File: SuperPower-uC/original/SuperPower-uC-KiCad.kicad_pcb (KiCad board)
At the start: 2 copper layers, 90 x 90 mm, 160 parts, among them J1 JST_PH_S2B_thru, J2 DNP/JST_ZH_S2B_thru, J3 JST_XH_S2B_thru, J4 mcu_pinout, J5 mcu_pinout, J601 Conn_01x02_Male, J8 Barrel_Jack_Switch, J9 DNP/Screw_Terminal_01x02, Q1 DMN2019UTS, Q2 DMN3018SSD, Q3 2N7002A, Q4 DMP3028LSD, Q5 S8050, Q6 S8050, Q7 2N7002A, Q701 DMP3028LSD, Q702 DMN3018SSD, Q703 2N7002A, Q8 DMP3028LSD, Q9 2N7002A, SW1 DNP/SKRKAEE020, U1 AP9101CK6-AYTRG1, U2 LTC4162EUFD-LAD, U3 USB-C, U4 CP2102N-A01-GQFN28, U5 ESP32-WROOM32, U601 RV-3028-C7, U701 TPS63070RNMT, U702 TPS63070RNMT, U703 TPS70933DRVT, U9 IP4220CZ6

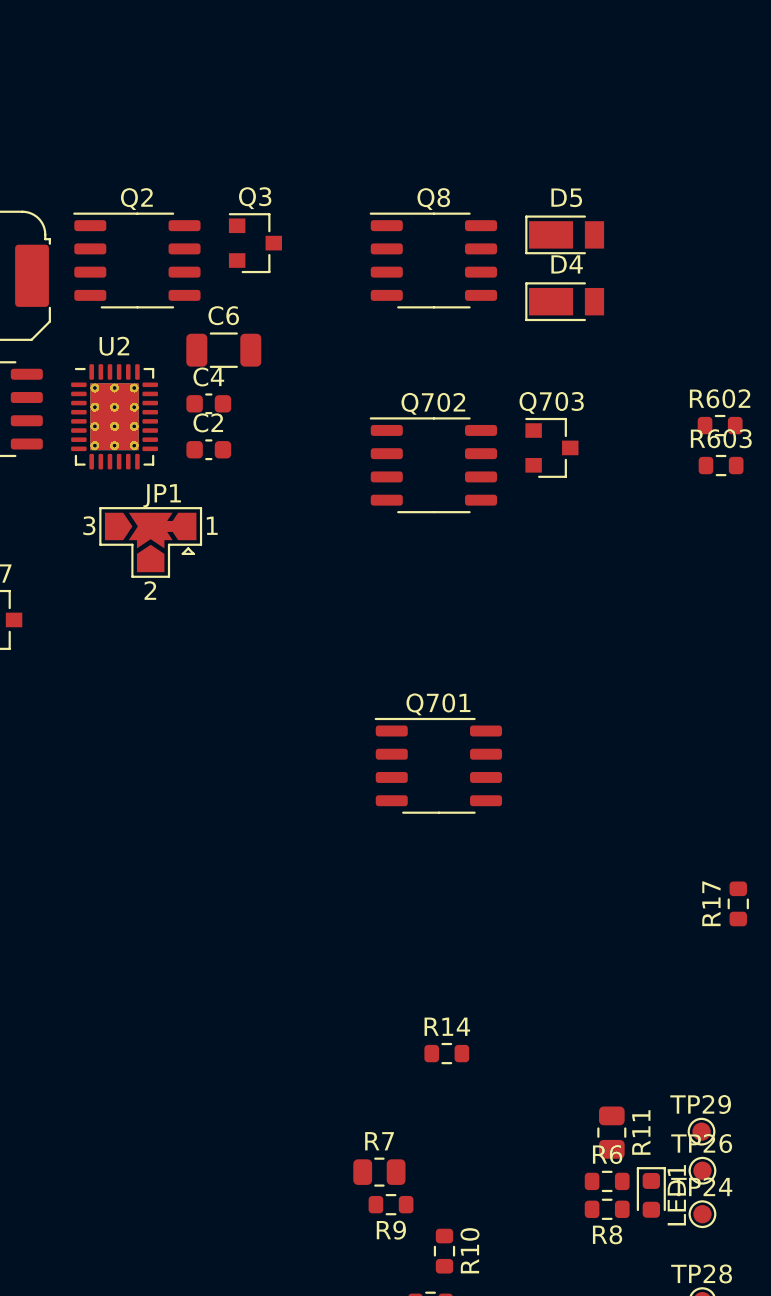
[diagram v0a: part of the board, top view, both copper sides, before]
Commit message: Update LTC4162-L Rsenses
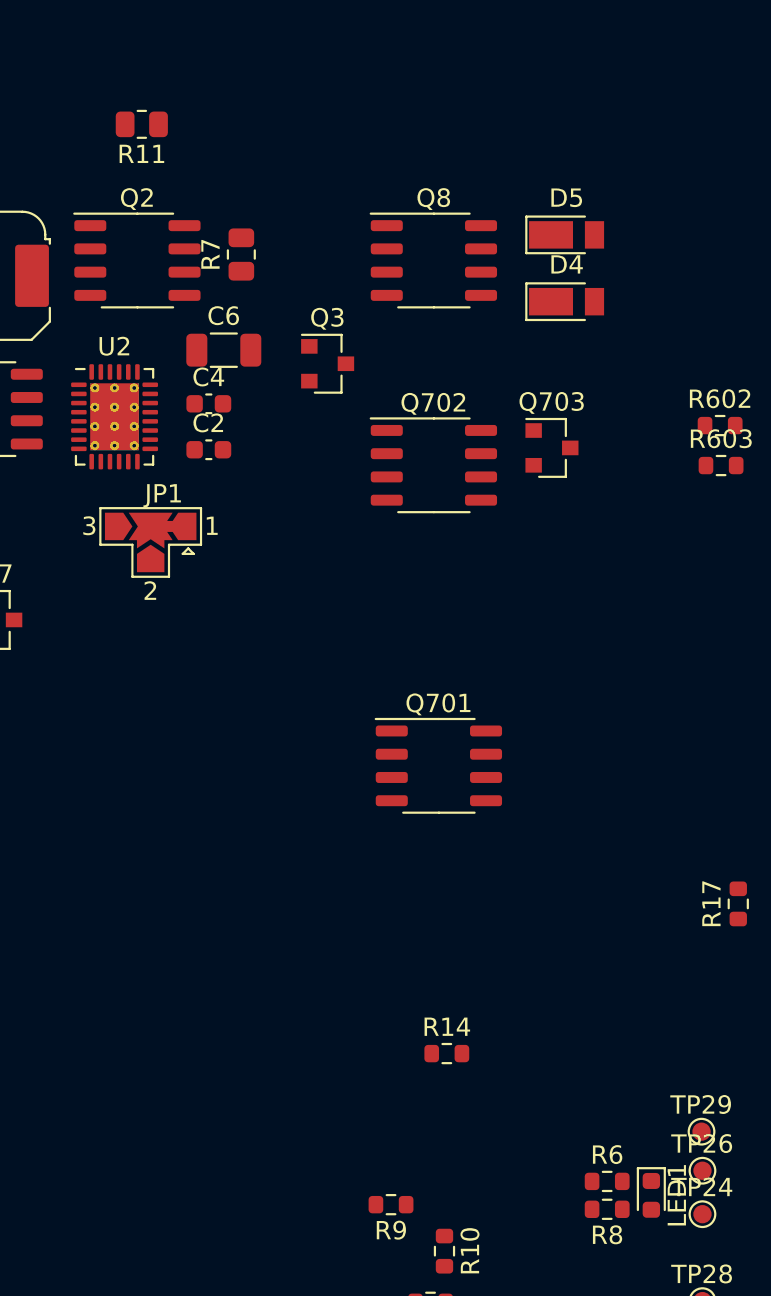
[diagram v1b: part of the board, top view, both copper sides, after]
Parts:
- R11, R7: value 68m -> RL0805FR-7W0R068L
- moved R11 60.8 mm to (68.1, 37.7), turned to 180 degrees
- moved R7 50.7 mm to (73.5, 44.8), turned to 90 degrees
- moved Q3 7.68 mm to (78.2, 50.8)
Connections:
- R11 pad 1: Net-(L1-Pad2) -> +BATT
- R11 pad 2: +BATT -> Net-(L1-Pad2)

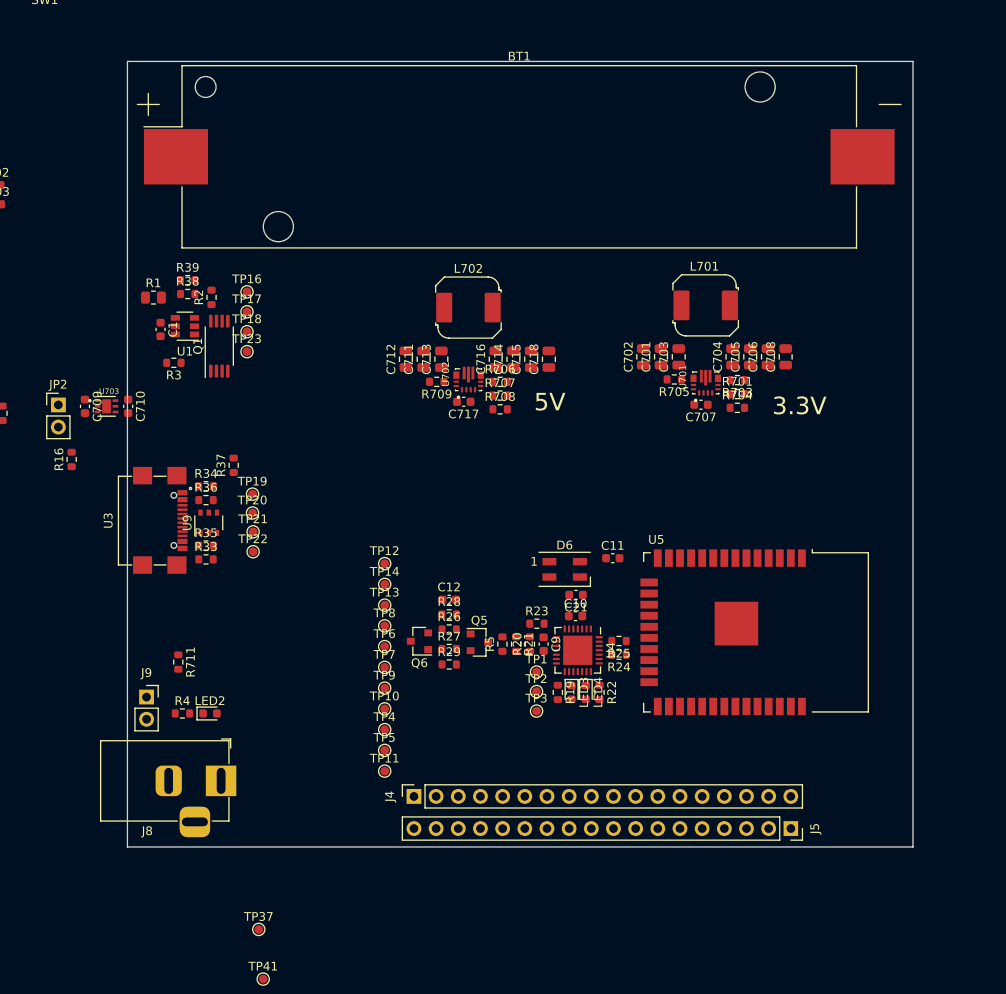
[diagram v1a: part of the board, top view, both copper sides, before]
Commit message: Add 3.2mm Mounting Holes (x4)
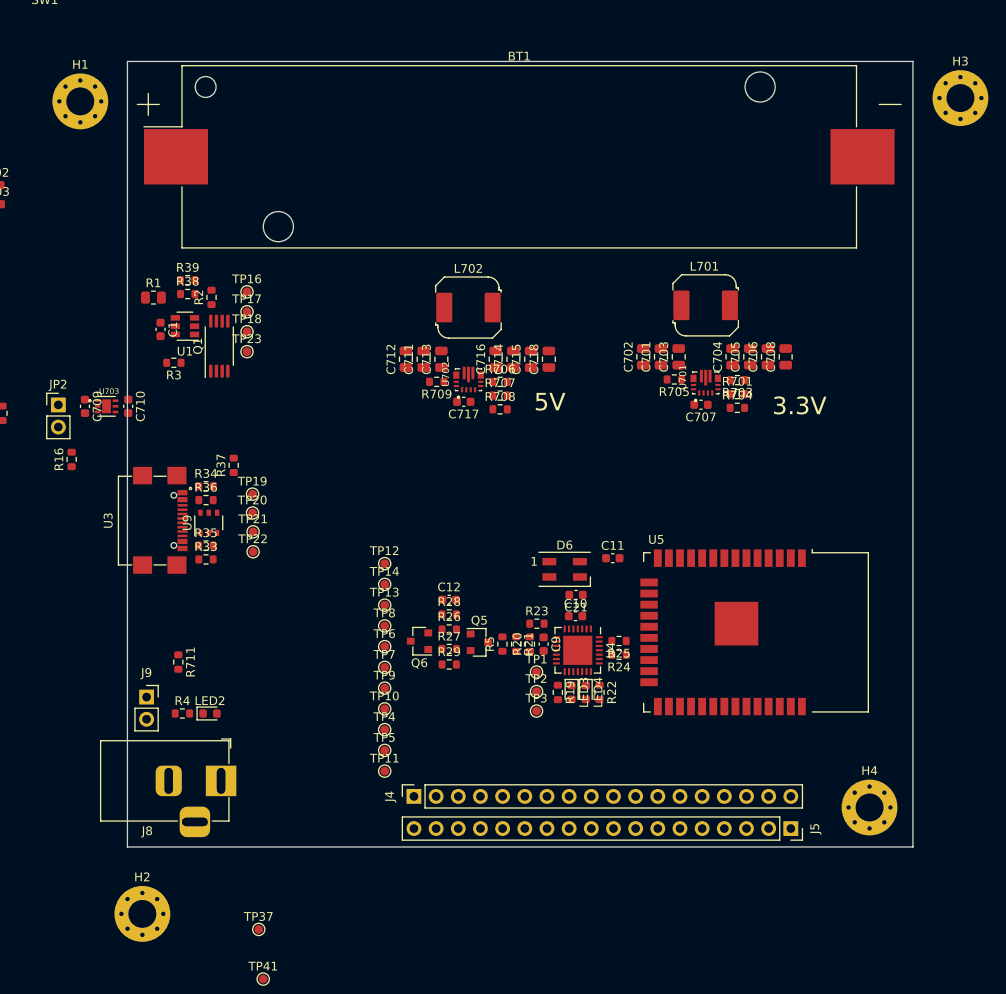
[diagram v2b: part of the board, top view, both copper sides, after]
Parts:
- added H1: MountingHole_Pad, MountingHole:MountingHole_3.2mm_M3_Pad_Via, F.Cu at (109.6, 44.6)
- added H2: MountingHole_Pad, MountingHole:MountingHole_3.2mm_M3_Pad_Via, F.Cu at (116.7, 137.7)
- added H3: MountingHole_Pad, MountingHole:MountingHole_3.2mm_M3_Pad_Via, F.Cu at (210.4, 44.2)
- added H4: MountingHole_Pad, MountingHole:MountingHole_3.2mm_M3_Pad_Via, F.Cu at (200.0, 125.5)

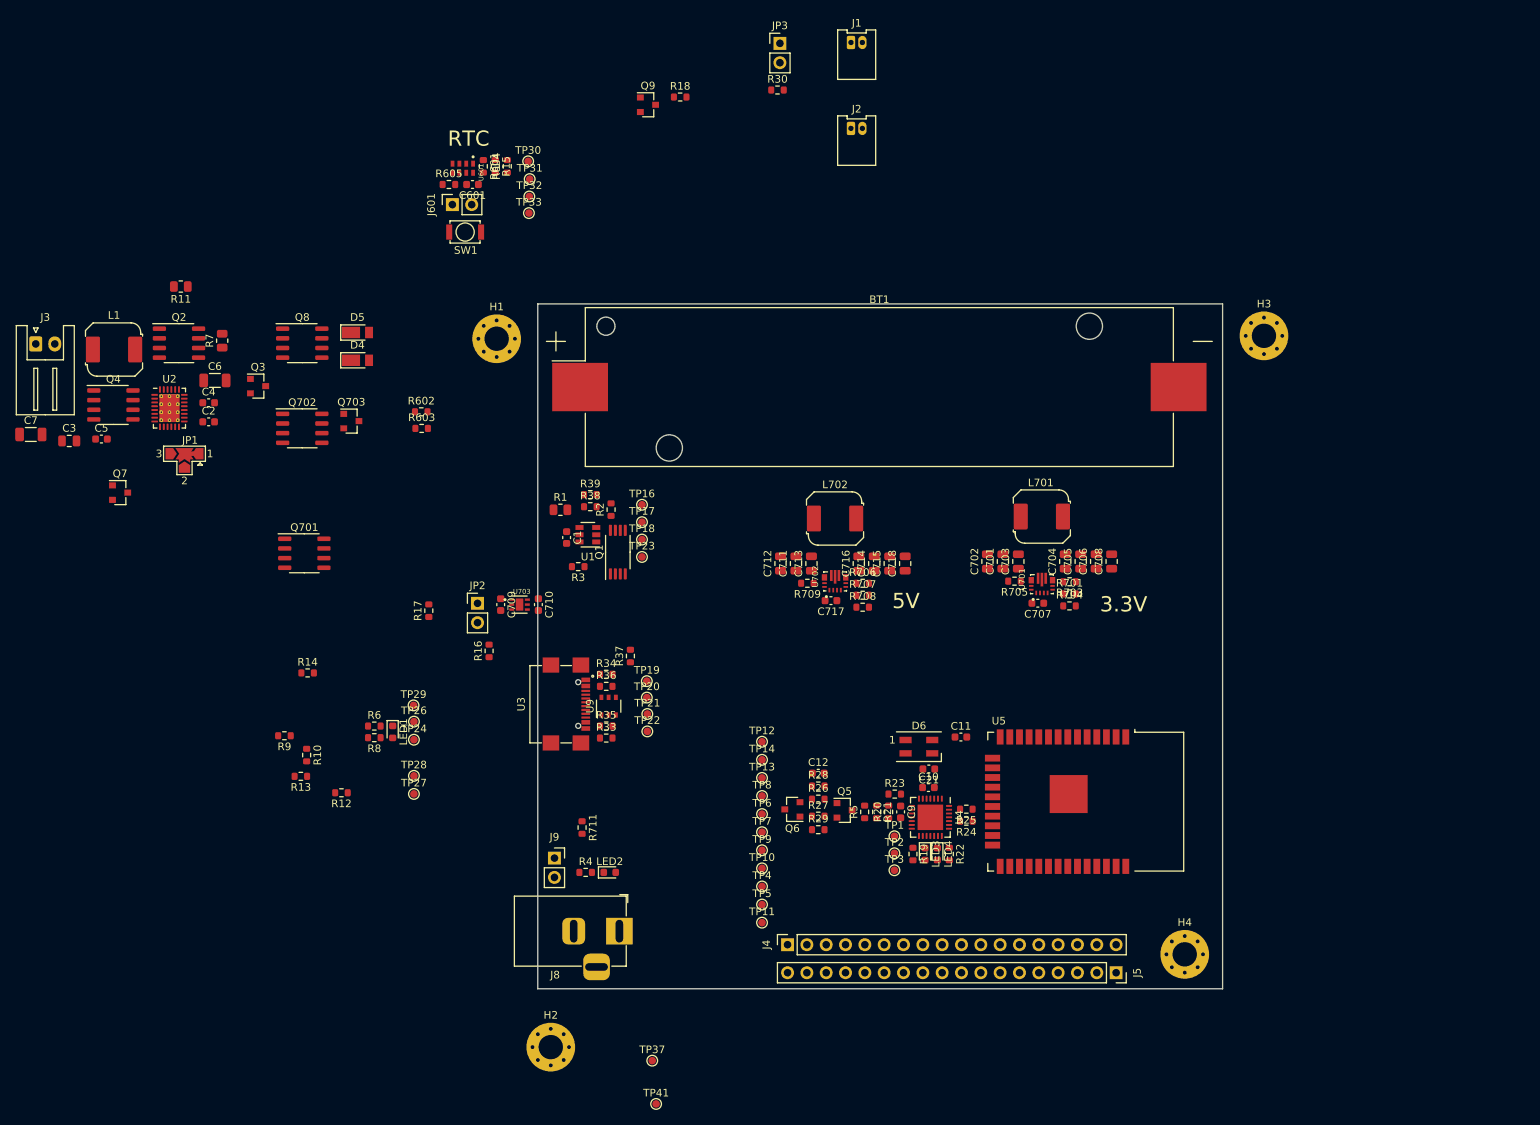
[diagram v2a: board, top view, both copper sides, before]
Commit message: Add battery break-out
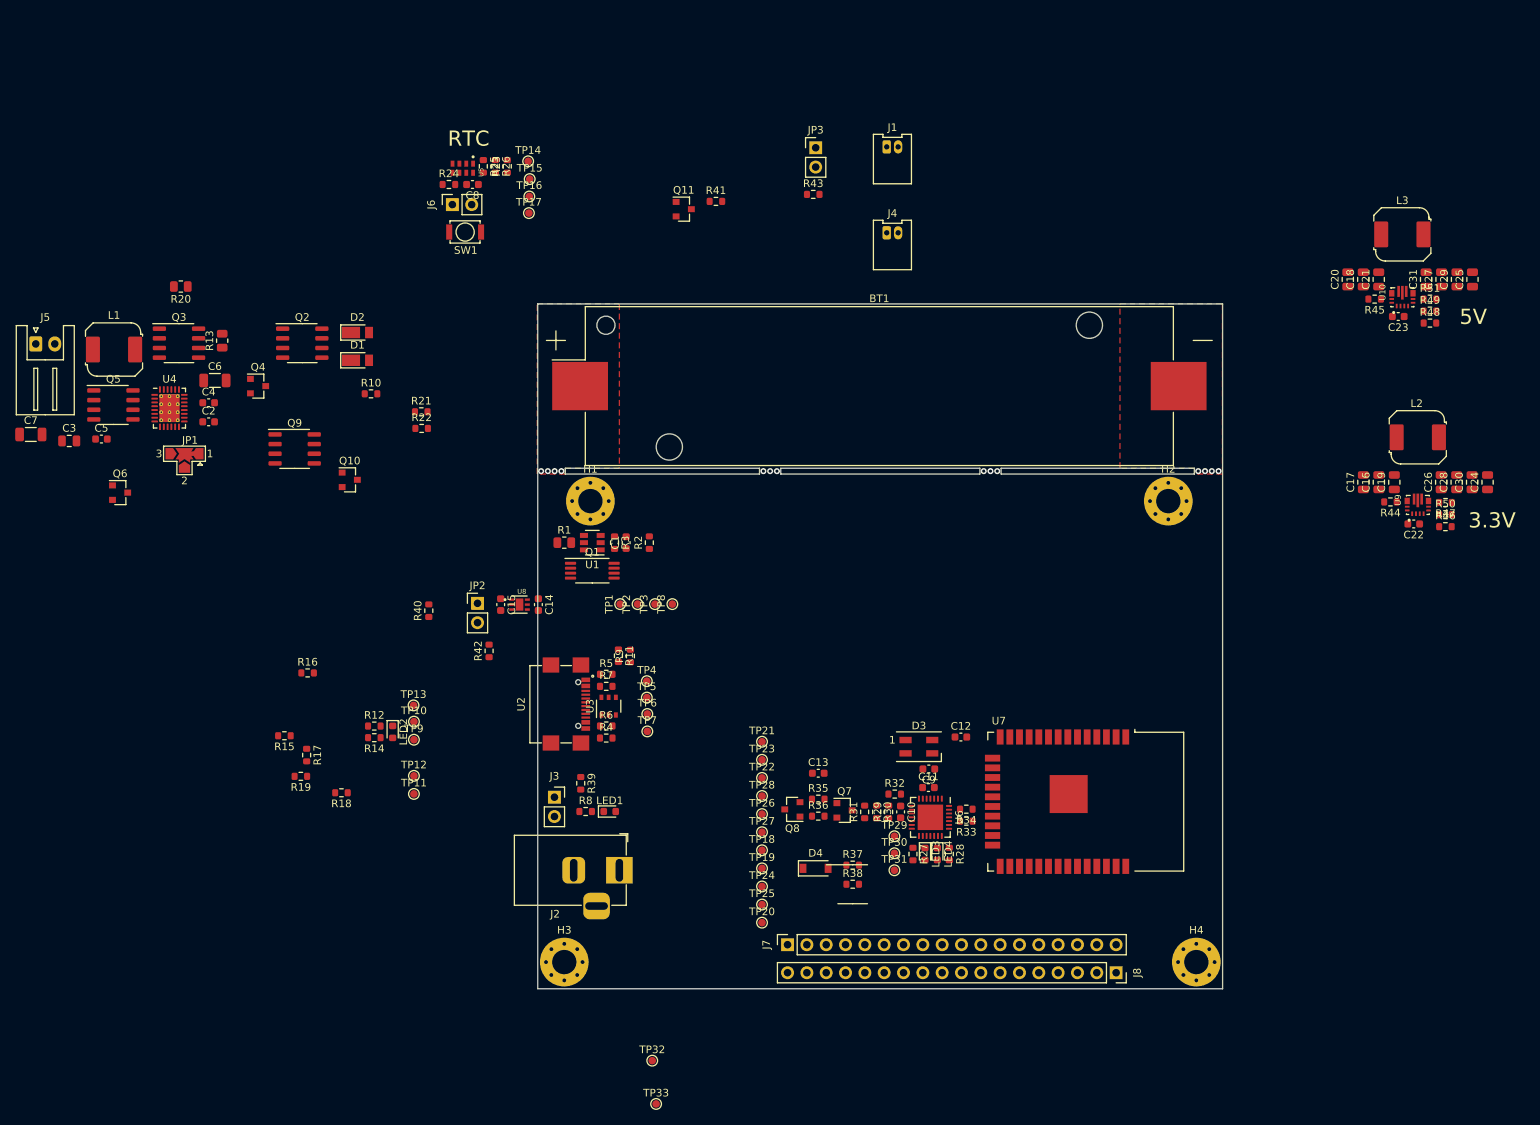
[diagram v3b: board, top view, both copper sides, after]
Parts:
- removed Q701: DMP3028LSD, Package_SO:SO-8_3.9x4.9mm_P1.27mm
- removed the R28 at (151.9, 103.4)
- removed the R29 at (151.9, 109.1)
- removed the U2 at (66.6, 53.7)
- added D4: B5819W, Diode_SMD:D_SOD-123, F.Cu at (151.5, 114.2)
- added R37: 12k, Resistor_SMD:R_0603_1608Metric, F.Cu at (156.4, 113.8)
- added R38: 12k, Resistor_SMD:R_0603_1608Metric, F.Cu at (156.4, 116.3)
- added U4: LTC4162EUFD-LAD, Package_DFN_QFN:QFN-28-1EP_4x5mm_P0.5mm_EP2.65x3.65mm_ThermalVias, F.Cu at (66.6, 53.7)
- moved C18 83.4 mm to (223.5, 36.8)
- moved C20 83.4 mm to (221.5, 36.8)
- moved C21 83.4 mm to (225.5, 36.8)
- moved C23 83.4 mm to (228.1, 41.7)
- moved C25 83.4 mm to (237.8, 36.8)
- moved C29 83.4 mm to (235.8, 36.8)
- moved C31 83.4 mm to (231.7, 36.8)
- moved L3 83.4 mm to (228.6, 30.9)
- moved R45 83.4 mm to (225.0, 39.4)
- moved U10 83.4 mm to (228.6, 39.1)
- moved R49 83.4 mm to (232.2, 40.9)
- moved C27 83.4 mm to (233.8, 36.8)
- moved R48 83.4 mm to (232.2, 42.5)
- moved R51 83.4 mm to (232.2, 39.4)
- moved C17 50.5 mm to (223.5, 63.4)
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- renumbered C9 to C10, C10 to C11, C11 to C12, C12 to C13, C710 to C14, C709 to C15, C701 to C16, C702 to C17, C711 to C18, C703 to C19, C712 to C20, C713 to C21, C707 to C22, C717 to C23, C708 to C24, C718 to C25, C704 to C26, C714 to C27, C705 to C28, C715 to C29, C706 to C30, C716 to C31, C601 to C8, C21 to C9, D4 to D1, D5 to D2, D6 to D3, H3 to H2, H2 to H3, J8 to J2, J9 to J3, J2 to J4, J3 to J5, J601 to J6, J4 to J7, J5 to J8, L701 to L2, L702 to L3, LED2 to LED1, LED1 to LED2, Q703 to Q10, Q9 to Q11, Q8 to Q2, Q2 to Q3, Q3 to Q4, Q4 to Q5, Q7 to Q6, Q5 to Q7, Q6 to Q8, Q702 to Q9, R38 to R10, R39 to R11, R6 to R12, R7 to R13, R8 to R14, R9 to R15, R14 to R16, R10 to R17, R12 to R18, R13 to R19, R3 to R2, R11 to R20, R602 to R21, R603 to R22, R604 to R23, R605 to R24, R601 to R25, R15 to R26, R19 to R27, R22 to R28, R20 to R29, R2 to R3, R21 to R30, R5 to R31, R23 to R32, R24 to R33, R25 to R34, R26 to R35, R27 to R36, R711 to R39, R33 to R4, R17 to R40, R18 to R41, R16 to R42, R30 to R43, R705 to R44, R709 to R45, R704 to R46, R703 to R47, R708 to R48, R707 to R49, R34 to R5, R701 to R50, R706 to R51, R35 to R6, R36 to R7, R4 to R8, R37 to R9, TP16 to TP1, TP26 to TP10, TP27 to TP11, TP28 to TP12, TP29 to TP13, TP30 to TP14, TP31 to TP15, TP32 to TP16, TP33 to TP17, TP9 to TP18, TP10 to TP19, TP17 to TP2, TP11 to TP20, TP12 to TP21, TP13 to TP22, TP14 to TP23, TP4 to TP24, TP5 to TP25, TP6 to TP26, TP7 to TP27, TP8 to TP28, TP1 to TP29, TP18 to TP3, TP2 to TP30, TP3 to TP31, TP37 to TP32, TP41 to TP33, TP19 to TP4, TP20 to TP5, TP21 to TP6, TP22 to TP7, TP23 to TP8, TP24 to TP9, U702 to U10, U3 to U2, U9 to U3, U601 to U5, U4 to U6, U5 to U7, U703 to U8, U701 to U9
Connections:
- C13 pad 1: /MCU Module/EN -> GND
- C13 pad 2: GND -> /MCU Module/EN
- C16 pad 1: Net-(C701-Pad1) -> Net-(C16-Pad1)
- C17 pad 1: Net-(C701-Pad1) -> Net-(C16-Pad1)
- C18 pad 1: Net-(C711-Pad1) -> Net-(C18-Pad1)
- C19 pad 1: Net-(C701-Pad1) -> Net-(C16-Pad1)
- C20 pad 1: Net-(C711-Pad1) -> Net-(C18-Pad1)
- C21 pad 1: Net-(C711-Pad1) -> Net-(C18-Pad1)
- Q5 pad 3: (no net) -> Net-(C16-Pad1)
- Q5 pad 4: (no net) -> Net-(JP2-Pad1)
- Q5 pad 5: (no net) -> /Regulator and Cut-Off Module/VIN
- Q5 pad 6: (no net) -> /Regulator and Cut-Off Module/VIN
- Q9 pad 1: Net-(C711-Pad1) -> GND
- Q9 pad 2: Net-(JP3-Pad1) -> /MCU Module/EN_3V3
- Q9 pad 3: GND -> Net-(C18-Pad1)
- Q9 pad 4: /MCU Module/EN_3V3 -> Net-(JP3-Pad1)
- Q9 pad 5: /Regulator and Cut-Off Module/GND_3v3 -> /Regulator and Cut-Off Module/VIN
- Q9 pad 6: /Regulator and Cut-Off Module/GND_3v3 -> /Regulator and Cut-Off Module/VIN
- Q9 pad 7: /Regulator and Cut-Off Module/VIN -> /Regulator and Cut-Off Module/GND_3v3
- Q9 pad 8: /Regulator and Cut-Off Module/VIN -> /Regulator and Cut-Off Module/GND_3v3
- R44 pad 2: Net-(C701-Pad1) -> Net-(C16-Pad1)
- R45 pad 2: Net-(C711-Pad1) -> Net-(C18-Pad1)
- U10 pad 12_13: Net-(C711-Pad1) -> Net-(C18-Pad1)
- U9 pad 12_13: Net-(C701-Pad1) -> Net-(C16-Pad1)
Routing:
- net -BATT: vias 0 -> 4
- net +BATT: vias 0 -> 4
- net (no net): vias 0 -> 6
- added copper zone on F.Cu, net +BATT
- added copper zone on F.Cu, net -BATT
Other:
- outline, holes or cut-outs redrawn
